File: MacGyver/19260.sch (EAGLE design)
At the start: 123 parts, among them J1 PST1,0/2-3,5, J10 RJ45J, J13 S04B, J2 PPPC101LFBN, J3 PPPC101LFBN, J4 PPPC101LFBN, J7 Pi Zero, J8 PST1,0/3-3,5, J9 RJ45J, Q1 IRFR5305, Q10 K38, Q11 K38, Q2 K1N, Q201 K1N, Q202 K1N, Q203 K1N, Q3 IRFR5305, Q4 P65, Q5 K3N, Q6 K1N, Q7 K3N, Q8 P65, Q9 K38, U1 1087, U10 Z4, U2 1087, U203 THVD1500, U204 THVD1500, U205 THVD1500, U3 I50115, U4 I50115, U5 AVR128DA28-I/SP, U6 AVR128DB32-I/PT, U7 Z4, U8 Z4, U9 Z4

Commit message: MacGyver: starting layout
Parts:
- removed C16, C17, C204, C205: .1uF, C-C:CC0603A
- removed J13: S04B, J-HDR2mm:B04B
- removed Q202: K1N, Q-NPN:NPNSOT23
- removed R202, R27, R28: 10k, R-C:R0805
- removed R203: 1.82k, R-C:R0805
- removed R221, R23, R24, R25, R26: 3.01k, R-C:R0805
- removed R224: 100k, R-C:R0805
- removed R227: 10K, R-C:R0805
- removed U10, U9: Z4, U-7400:2G07SOT26
- added C103, C104, C106, C107: .1uF, C-C:CC0603A
- added C108, C109: 27pF, C-C:CC0603A
- added J5: Pi Zero, U-Pi:RPI-ZERO90
- added Q102: K1N, Q-NPN:NPNSOT23
- added R101, R117, R118: 10k, R-C:R0805
- added R102, R105, R106, R107: 3.01k, R-C:R0805
- added R103: 1.82k, R-C:R0805
- added R112: 100k, R-C:R0805
- added U101: Z4, U-7400:2G07SOT26
- added U106: AVR128DB32-I/PT, U-AVR:AVR128DB32
- added Y1: 16MHz, Y-XTL:CSM-3X
- J7: value Pi Zero -> S04B; device U-Pi:RPI-ZERO90 -> J-HDR2mm:B04B
- Q2: value K1N -> IRFR5305; device Q-NPN:NPNSOT23 -> Q-PCH:N-CHDPAK
- Q3: value IRFR5305 -> P65; device Q-PCH:N-CHDPAK -> Q-PCH:N-CHSOT23
- Q4: value P65 -> K3N; device Q-PCH:N-CHSOT23 -> Q-PNP:PNPSOT23
- Q5: value K3N -> K1N; device Q-PNP:PNPSOT23 -> Q-NPN:NPNSOT23
- Q6: value K1N -> K3N; device Q-NPN:NPNSOT23 -> Q-PNP:PNPSOT23
- Q7: value K3N -> P65; device Q-PNP:PNPSOT23 -> Q-PCH:N-CHSOT23
- Q8: value P65 -> K38; device Q-PCH:N-CHSOT23 -> Q-NCH:N-CHSOT23
- Q9: value K38 -> K1N; device Q-NCH:N-CHSOT23 -> Q-NPN:NPNSOT23
- R10: value 10k -> 80.6k
- R11: value 100k -> 10k
- R12: value 80.6k -> 100k
- R14: value 10k -> 49.9k
- R15: value 49.9k -> 10k
- R18: value 1.82k -> 10k
- R2: value 100k -> 0.010; device R-C:R0805 -> R-C:R1210
- R21: value 10k -> 3.01k
- R3: value 0.010 -> 1K; device R-C:R1210 -> R-C:R0805
- R4, R9: value 10k -> 100k
- R5: value 1K -> 15.8k
- R6: value 100k -> 0.068; device R-C:R0805 -> R-C:R1210
- R7: value 15.8k -> 10k
- R8: value 0.068 -> 10k; device R-C:R1210 -> R-C:R0805
- U5: value AVR128DA28-I/SP -> Z4; device U-AVR:AVR128DA28-I/SP -> U-7400:2G07SOT26
- U6: value AVR128DB32-I/PT -> AVR128DA28-I/SP; device U-AVR:AVR128DB32 -> U-AVR:AVR128DA28-I/SP
- renumbered C201 to C101, C202 to C102, C203 to C105, C208 to C110, D2 to D1, D202 to D101, J8 to J6, Q201 to Q101, Q203 to Q103, R212 to R108, R213 to R110, R214 to R104, R215 to R114, R222 to R109, R223 to R120, R225 to R111, R226 to R113, R229 to R124, R230 to R125, R231 to R126, R232 to R127, R233 to R119, R234 to R121, R235 to R122, R236 to R123, R237 to R116, R238 to R115, R239 to R128, U203 to U102, U204 to U104, U205 to U105, U8 to U103
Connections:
- removed net PI_RX0: J7.RXD/BCM15, R18.2, R203.1, U103B.O, U6.(TX1)PC0, U7B.O
- removed net PI_TX0: J7.TXD/BCM14, R202.2, U103A.I, U6.(RX1)PC1, U7A.I
- removed net UPDI-APP: J4.8, R26.1, U10B.I, U5.UPDI
- new net APP_UPDI: J3.8, R21.1, U6.UPDI, U7B.I
- new net PI_RX: J5.RXD/BCM15, R103.2, U101B.O, U103B.O, U106.(TX1)PC0
- new net PI_TX: J5.TXD/BCM14, R101.2, U101A.I, U103A.I, U106.(RX1)PC1
- net !RESET: now also J3.5, U6.PF6(!RESET); no longer J4.5, U5.PF6(!RESET)
- net !SS: now also J2.8, U6.(!SS!)PA7; no longer J3.8, U5.(!SS!)PA7
- net +5V: now also C106.1, C107.1, C14.1, J7.3, R102.1, R105.1, R20.1, R8.2, U106.AVDD, U106.VDD, U6.AVCC, U6.VCC@0; no longer C12.1, C204.1, C205.1, J13.3, R10.2, R227.1, R23.1, R24.1, R25.1, U5.AVCC, U5.VCC@0, U6.AVDD, U6.VDD
- net +5V_2PI: now also J5.5V0@1, J5.5V0@2; no longer J7.5V0@1, J7.5V0@2
- net 0V: now also C103.2, C104.2, C106.2, C107.2, C108.1, C109.1, J5.GND@1, J5.GND@2, J5.GND@3, J5.GND@4, J5.GND@5, J5.GND@6, J5.GND@7, J5.GND@8, J7.4, Q102.E, Q8.S, R107.1, R11.1, R117.2, R118.2, R13.2, R18.2, R5.1, U101P.GND, U106.0V@0, U106.0V@1, U5P.GND; no longer C16.2, C17.2, C204.2, C205.2, J13.4, J7.GND@1, J7.GND@2, J7.GND@3, J7.GND@4, J7.GND@5, J7.GND@6, J7.GND@7, J7.GND@8, Q202.E, Q9.S, R13.1, R14.2, R21.2, R221.1, R27.2, R28.2, R7.1, U10P.GND, U5.0V@0, U5.0V@1, U9P.GND
- net AIN0: now also J4.3, U6.(AIN0)PD0; no longer J2.3, U5.(AIN0)PD0
- net AIN1: now also J4.4, U6.(AIN1)PD1; no longer J2.4, U5.(AIN1)PD1
- net AIN2: now also J4.5, U6.(AIN2)PD2; no longer J2.5, U5.(AIN2)PD2
- net AIN3: now also J4.6, U6.(AIN3)PD3; no longer J2.6, U5.(AIN3)PD3
- net AIN4: now also J4.7, U6.(AIN4)PD4; no longer J2.7, U5.(AIN4)PD4
- net AIN5: now also J4.8, U6.(AIN5)PD5; no longer J2.8, U5.(AIN5)PD5
- net AIN6: now also J4.9, U6.(AIN6)PD6; no longer J2.9, U5.(AIN6)PD6
- net AIN7: now also J4.10, U6.(AREF)PD7; no longer J2.10, U5.(AREF)PD7
- net ALT_EN: now also R13.1, U106.(AIN5)PD5; no longer R14.1, U6.(AIN5)PD5
- net ALT_I: now also R15.1, U106.(AIN1)PD1; no longer R4.1, U6.(AIN1)PD1
- net ALT_V: now also R11.2, U106.(AIN2)PD2; no longer R13.2, U6.(AIN2)PD2
- net APP_RX0: now also J3.7, R17.2, U5A.O, U6.(RX0)PA1; no longer J4.7, R23.2, U5.(RX0)PA1, U9A.O
- net APP_TX0: now also J3.6, U5B.I, U6.(EXTCLK/TX0)PA0; no longer J4.6, U5.(EXTCLK/TX0)PA0, U9B.I
- net APP_UART_: now also C12.1, R18.1, U106.(SDA0)PA2, U5P.VCC; no longer C16.1, R27.1, U6.(SDA0)PA2, U9P.VCC
- net APP_UPDI_: now also C15.1, R22.1, U106.(SCL0)PA3, U7P.VCC; no longer C17.1, R28.1, U10P.VCC, U6.(SCL0)PA3
- net FROM_RPU_OOB: now also U106.PF1(RX2); no longer U6.PF1(RX2)
- net FROM_RPU_RX: now also U5A.I, U7A.I; no longer U10A.I, U9A.I
- net FROM_RPU_TX: now also U101B.I; no longer U7B.I
- net I2C_SCL: now also J2.4, J7.1, U6.(SCL0)PA3; no longer J13.1, J3.4, U5.(SCL0)PA3
- net I2C_SCL_: now also U106.PF3(SCL1); no longer U6.PF3(SCL1)
- net I2C_SDA: now also J2.3, J7.2, U6.(SDA0)PA2; no longer J13.2, J3.3, U5.(SDA0)PA2
- net I2C_SDA_: now also U106.PF2(SDA1); no longer U6.PF2(SDA1)
- net MGR_LED: now also U106.(AREF)PD7; no longer U6.(AREF)PD7
- net MGR_UPDI: now also R106.1, U106.UPDI; no longer R20.1, U6.UPDI
- net MISO: now also J2.6, U6.(MISO)PA5; no longer J3.6, U5.(MISO)PA5
- net MOSI: now also J2.5, U6.(MOSI)PA4; no longer J3.5, U5.(MOSI)PA4
- net N$1: now also R105.2, R106.2; no longer R19.2, R20.2
- net N$10: now also Q4.E, Q6.B, R3.1; no longer Q5.E, Q7.B, R5.1
- net N$11: now also C109.2, U106.PA0(XTALHF1), Y1.2; no longer U6.PA0(XTALHF1)
- net N$2: now also Q7.G, R10.1, R9.2; no longer Q8.G, R11.2, R12.1
- net N$3: now also R20.2, R21.2, U7A.O; no longer R25.2, R26.2, U10A.O
- net N$32: now also Q2.S, Q9.E, R12.2, R2.1; no longer Q2.E, Q3.S, R2.2, R3.1
- net N$33: now also Q2.G, Q9.B, Q9.C, R12.1, R14.2; no longer Q2.B, Q2.C, Q3.G, R15.2, R2.1
- net N$34: now also R14.1; no longer R15.1
- net N$4: now also Q8.D, R10.2; no longer Q9.D, R12.2
- net N$5: now also Q4.B, Q6.C; no longer Q5.B, Q7.C
- net N$6: now also Q3.G, Q5.B, Q5.C, Q6.E, R3.2; no longer Q4.G, Q6.B, Q6.C, Q7.E, R5.2
- net N$65: now also R15.2; no longer R4.2
- net N$66: now also R2.2; no longer R3.2
- net N$7: now also Q4.C; no longer Q5.C
- net N$8: now also R7.2; no longer R9.2
- net N$83: now also Q102.C; no longer Q202.C
- net N$84: now also Q102.B, R112.1; no longer Q202.B, R224.1
- net N$9: now also C108.2, U106.PA1(XTALHF2), Y1.1; no longer U6.PA1(XTALHF2)
- net OOB_!RE: now also R107.2, U106.(SCK)PA6; no longer R221.2, U6.(SCK)PA6
- net OOB_DE: now also U106.(!SS!)PA7; no longer U6.(!SS!)PA7
- net PC2: now also J3.9, U6.PC2; no longer J4.9, U5.PC2
- net PC3: now also J3.10, U6.PC3; no longer J4.10, U5.PC3
- net PI3V3: now also J5.3V3@1, R101.1, R103.1, U106.VDDIO2; no longer J7.3V3@1, R18.1, R202.1, R203.2, U6.VDDIO2
- net PIPWR_EN: now also Q8.G, R8.1, U106.(AIN6)PD6; no longer Q9.G, R10.1, U6.(AIN6)PD6
- net PI_UART_TO_MGR_UPDI: now also C104.1, J5.SD_DAT0/BCM24, R118.1; no longer C15.1, J7.SD_DAT0/BCM24, R22.1
- net PI_UART_TO_RPU: now also C103.1, J5.SD_CMD/BCM23, R117.1, U101P.VCC; no longer C14.1, J7.SD_CMD/BCM23, R21.1, U7P.VCC
- net POWER: now also Q2.D; no longer Q4.D
- net PWR_I: now also R7.1, U106.(AIN3)PD3; no longer R9.1, U6.(AIN3)PD3
- net PWR_V: now also R4.1, R5.2, U106.(AIN4)PD4; no longer R6.1, R7.2, U6.(AIN4)PD4
- net RX1: now also J2.10, U6.(RX1)PC1; no longer J3.10, U5.(RX1)PC1
- net RX2: now also J3.4, U6.PF1(RX2); no longer J4.4, U5.PF1(RX2)
- net RX_!RE: now also U106.(MOSI)PA4; no longer U6.(MOSI)PA4
- net RX_DE: now also U106.PF4(AIN20); no longer U6.PF4(AIN20)
- net RX_RPU: no longer R227.2
- net SCK: now also J2.7, U6.(SCK)PA6; no longer J3.7, U5.(SCK)PA6
- net SHLD_VIN: now also Q7.D; no longer Q8.D
- net SHUTDWN: now also U106.PF6(!RESET); no longer U6.PF6(!RESET)
- net SHUTDWN_TO_BCM6: now also J5.BCM6; no longer J7.BCM6
- net SMBUS_SCL: now also J5.BCM3/SCL, U106.(*SCL0)PC3; no longer J7.BCM3/SCL, U6.(*SCL0)PC3
- net SMBUS_SDA: now also J5.BCM2/SDA, U106.(*SDA0)PC2; no longer J7.BCM2/SDA, U6.(*SDA0)PC2
- net TO_RPU_OOB: now also R112.2, U106.PF0(TX2); no longer R224.2, U6.PF0(TX2)
- net TO_RPU_RX: now also R102.2, U101A.O; no longer R17.2, U7A.O
- net TO_RPU_TX: now also R19.2, U5B.O, U7B.O; no longer R24.2, U10B.O, U9B.O
- net TX1: now also J2.9, U6.(TX1)PC0; no longer J3.9, U5.(TX1)PC0
- net TX2: now also J3.3, U6.PF0(TX2); no longer J4.3, U5.PF0(TX2)
- net TX_!RE: now also U106.PF5(AIN21); no longer U6.PF5(AIN21)
- net TX_DE: now also U106.(MISO)PA5; no longer U6.(MISO)PA5
- net VIN: now also Q7.S, R6.1, R9.1; no longer Q8.S, R11.1, R8.1
- net VIN_S: now also Q3.S, Q5.E, R4.2; no longer Q4.S, Q6.E, R8.2
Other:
- note added: "R-PI TO MGR_UPDI"
- note added: "R-PI TO RPU"
- note added: "RPU TO APPLICATION"
- note added: "RPU TO APP_UPDI"
- note removed: "MGR UPDI TO R-PI"
- note removed: "RPU TX/RX TO R-PI"
- note removed: "UART_0 TO APPLICATION"

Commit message: MacGyver: layout wip
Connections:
- net ALT_EN: now also U106.(SCL0)PA3; no longer U106.(AIN5)PD5
- net APP_UART_: now also U106.PF4(AIN20); no longer U106.(SDA0)PA2
- net APP_UPDI_: now also U106.PF5(AIN21); no longer U106.(SCL0)PA3
- net PIPWR_EN: now also U106.(SDA0)PA2; no longer U106.(AIN6)PD6
- net RX_!RE: now also U106.(AIN5)PD5; no longer U106.(MOSI)PA4
- net RX_DE: now also U106.(AIN6)PD6; no longer U106.PF4(AIN20)
- net TX_!RE: now also U106.(MOSI)PA4; no longer U106.PF5(AIN21)
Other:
- note removed: "15"
- note removed: "2"
- note removed: "25"
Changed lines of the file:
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@@
 <text x="335.788" y="44.196" size="2.1844" layer="98">11/12/20</text>
 <text x="356.616" y="19.558" size="2.54" layer="98">MACGYVER</text>
-<text x="106.934" y="94.488" size="1.27" layer="98">2</text>
-<text x="106.934" y="51.308" size="1.27" layer="98">15</text>
 <text x="109.474" y="43.688" size="1.27" layer="98">17</text>
-<text x="51.054" y="58.928" size="1.27" layer="98">25</text>
 <text x="119.634" y="76.454" size="2.54" layer="98">debug</text>
 <text x="372.364" y="190.754" size="2.54" layer="98">OUT OF BAND</text>
@@
 <segment>
 <pinref part="C109" gate="G$1" pin="1"/>
-<wire x1="43.18" y1="76.2" x2="40.64" y2="76.2" width="0.1524" layer="91"/>
-<wire x1="40.64" y1="76.2" x2="40.64" y2="83.82" width="0.1524" layer="91"/>
+<wire x1="43.18" y1="76.2" x2="38.1" y2="76.2" width="0.1524" layer="91"/>
+<wire x1="38.1" y1="76.2" x2="38.1" y2="83.82" width="0.1524" layer="91"/>
 <pinref part="GND14" gate="1" pin="0V"/>
-<wire x1="40.64" y1="83.82" x2="43.18" y2="83.82" width="0.1524" layer="91"/>
+<wire x1="38.1" y1="83.82" x2="43.18" y2="83.82" width="0.1524" layer="91"/>
 <pinref part="C108" gate="G$1" pin="1"/>
-<wire x1="43.18" y1="86.36" x2="40.64" y2="86.36" width="0.1524" layer="91"/>
-<wire x1="40.64" y1="86.36" x2="40.64" y2="83.82" width="0.1524" layer="91"/>
-<junction x="40.64" y="83.82"/>
+<wire x1="43.18" y1="86.36" x2="38.1" y2="86.36" width="0.1524" layer="91"/>
+<wire x1="38.1" y1="86.36" x2="38.1" y2="83.82" width="0.1524" layer="91"/>
+<junction x="38.1" y="83.82"/>
 </segment>
 </net>
@@
 </segment>
 <segment>
-<label x="109.22" y="93.98" size="1.27" layer="91" xref="yes"/>
-<wire x1="99.06" y1="93.98" x2="109.22" y2="93.98" width="0.1524" layer="91"/>
-<pinref part="U106" gate="G$1" pin="(MOSI)PA4"/>
+<label x="109.22" y="50.8" size="1.27" layer="91" xref="yes"/>
+<wire x1="99.06" y1="50.8" x2="109.22" y2="50.8" width="0.1524" layer="91"/>
+<pinref part="U106" gate="G$1" pin="(AIN5)PD5"/>
 </segment>
 </net>
@@
 </segment>
 <segment>
-<label x="50.8" y="58.42" size="1.27" layer="91" rot="MR0" xref="yes"/>
-<wire x1="60.96" y1="58.42" x2="50.8" y2="58.42" width="0.1524" layer="91"/>
-<pinref part="U106" gate="G$1" pin="PF5(AIN21)"/>
+<label x="109.22" y="93.98" size="1.27" layer="91" rot="MR180" xref="yes"/>
+<wire x1="109.22" y1="93.98" x2="99.06" y2="93.98" width="0.1524" layer="91"/>
+<pinref part="U106" gate="G$1" pin="(MOSI)PA4"/>
 </segment>
 </net>
@@
 </segment>
 <segment>
-<label x="50.8" y="60.96" size="1.27" layer="91" rot="MR0" xref="yes"/>
-<wire x1="60.96" y1="60.96" x2="50.8" y2="60.96" width="0.1524" layer="91"/>
-<pinref part="U106" gate="G$1" pin="PF4(AIN20)"/>
+<label x="109.22" y="48.26" size="1.27" layer="91" rot="MR180" xref="yes"/>
+<wire x1="99.06" y1="48.26" x2="109.22" y2="48.26" width="0.1524" layer="91"/>
+<pinref part="U106" gate="G$1" pin="(AIN6)PD6"/>
 </segment>
 </net>
@@
 <net name="ALT_EN" class="0">
 <segment>
-<label x="109.22" y="50.8" size="1.27" layer="91" xref="yes"/>
-<wire x1="99.06" y1="50.8" x2="109.22" y2="50.8" width="0.1524" layer="91"/>
-<pinref part="U106" gate="G$1" pin="(AIN5)PD5"/>
+<label x="109.22" y="96.52" size="1.27" layer="91" xref="yes"/>
+<wire x1="99.06" y1="96.52" x2="109.22" y2="96.52" width="0.1524" layer="91"/>
+<pinref part="U106" gate="G$1" pin="(SCL0)PA3"/>
 </segment>
 </net>
@@
 <net name="PIPWR_EN" class="0">
 <segment>
-<label x="109.22" y="48.26" size="1.27" layer="91" xref="yes"/>
-<wire x1="99.06" y1="48.26" x2="109.22" y2="48.26" width="0.1524" layer="91"/>
-<pinref part="U106" gate="G$1" pin="(AIN6)PD6"/>
+<label x="109.22" y="99.06" size="1.27" layer="91" xref="yes"/>
+<wire x1="99.06" y1="99.06" x2="109.22" y2="99.06" width="0.1524" layer="91"/>
+<pinref part="U106" gate="G$1" pin="(SDA0)PA2"/>
 </segment>
 </net>
@@
 <segment>
 <label x="109.22" y="53.34" size="1.27" layer="91" xref="yes"/>
+<pinref part="U106" gate="G$1" pin="(AIN4)PD4"/>
 <wire x1="99.06" y1="53.34" x2="109.22" y2="53.34" width="0.1524" layer="91"/>
-<pinref part="U106" gate="G$1" pin="(AIN4)PD4"/>
 </segment>
 </net>
@@
 <net name="APP_UART_" class="0">
 <segment>
-<pinref part="U106" gate="G$1" pin="(SDA0)PA2"/>
-<wire x1="99.06" y1="99.06" x2="109.22" y2="99.06" width="0.1524" layer="91"/>
-<label x="109.22" y="99.06" size="1.27" layer="91" xref="yes"/>
+<label x="50.8" y="60.96" size="1.27" layer="91" rot="R180" xref="yes"/>
+<wire x1="60.96" y1="60.96" x2="50.8" y2="60.96" width="0.1524" layer="91"/>
+<pinref part="U106" gate="G$1" pin="PF4(AIN20)"/>
 </segment>
 </net>
 <net name="APP_UPDI_" class="0">
 <segment>
-<pinref part="U106" gate="G$1" pin="(SCL0)PA3"/>
-<wire x1="99.06" y1="96.52" x2="109.22" y2="96.52" width="0.1524" layer="91"/>
-<label x="109.22" y="96.52" size="1.27" layer="91" xref="yes"/>
-</segment>
-</net>
+<label x="50.8" y="58.42" size="1.27" layer="91" rot="R180" xref="yes"/>
+<wire x1="50.8" y1="58.42" x2="60.96" y2="58.42" width="0.1524" layer="91"/>
+<pinref part="U106" gate="G$1" pin="PF5(AIN21)"/>
+</segment>
+</net>

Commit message: MacGyver: layout wip++
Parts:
- removed TP2, TP3: TPPAD1-08, J-TP:TPPAD1-08
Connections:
- net N$1 renamed MGR_UPDI_PULLUP
- net N$3 renamed APP_UPDI_PULLUP
- net I2C_SCL: no longer TP2.TP
- net I2C_SDA: no longer TP1.TP
- net MGR_UPDI: now also TP1.TP; no longer TP3.TP
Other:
- moved on the sheet: TP1
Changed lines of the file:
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@@
 <part name="Q1" library="Q-PCH" deviceset="N-CH?*" device="DPAK" value="IRFR5305"/>
 <part name="Q11" library="Q-NCH" deviceset="N-CH?*" device="SOT23" value="K38"/>
-<part name="TP1" library="J-TP" deviceset="TP" device="PAD1-08"/>
-<part name="TP2" library="J-TP" deviceset="TP" device="PAD1-08"/>
 <part name="J4" library="J-HDR2.54mm" deviceset="F1X10" device="" value="PPPC101LFBN"/>
 <part name="J2" library="J-HDR2.54mm" deviceset="F1X10" device="" value="PPPC101LFBN"/>
@@
 <part name="R18" library="R-C" deviceset="R" device="0805" value="10k"/>
 <part name="R22" library="R-C" deviceset="R" device="0805" value="10k"/>
-<part name="TP3" library="J-TP" deviceset="TP" device="PAD1-08"/>
+<part name="TP1" library="J-TP" deviceset="TP" device="PAD1-08"/>
 <part name="R19" library="R-C" deviceset="R" device="0805" value="3.01k"/>
 <part name="P+10" library="Plane" deviceset="+5V" device=""/>
@@
 </segment>
 </net>
-<net name="N$3" class="0">
+<net name="APP_UPDI_PULLUP" class="0">
 <segment>
 <pinref part="U7" gate="A" pin="O"/>
@@
 <instance part="P+29" gate="1" x="121.92" y="27.94"/>
 <instance part="P+31" gate="1" x="210.82" y="86.36"/>
-<instance part="TP1" gate="G$1" x="215.9" y="78.74"/>
-<instance part="TP2" gate="G$1" x="215.9" y="68.58"/>
 <instance part="GND1" gate="1" x="22.86" y="83.82"/>
 <instance part="GND4" gate="1" x="30.48" y="81.28"/>
@@
 <instance part="R117" gate="G$1" x="86.36" y="137.16" rot="R270"/>
 <instance part="R118" gate="G$1" x="124.46" y="137.16" rot="R270"/>
-<instance part="TP3" gate="G$1" x="58.42" y="93.98"/>
+<instance part="TP1" gate="G$1" x="58.42" y="93.98"/>
 <instance part="C108" gate="G$1" x="45.72" y="86.36" smashed="yes" rot="R90">
 <attribute name="NAME" x="48.006" y="86.995" size="1.778" layer="95"/>
@@
 <segment>
 <label x="220.98" y="73.66" size="1.27" layer="91" xref="yes"/>
-<wire x1="220.98" y1="73.66" x2="215.9" y2="73.66" width="0.1524" layer="91"/>
 <pinref part="R126" gate="G$1" pin="1"/>
-<wire x1="215.9" y1="73.66" x2="198.12" y2="73.66" width="0.1524" layer="91"/>
+<wire x1="220.98" y1="73.66" x2="198.12" y2="73.66" width="0.1524" layer="91"/>
 <wire x1="198.12" y1="73.66" x2="195.58" y2="73.66" width="0.1524" layer="91"/>
 <wire x1="198.12" y1="78.74" x2="198.12" y2="73.66" width="0.1524" layer="91"/>
 <junction x="198.12" y="73.66"/>
 <pinref part="R124" gate="G$1" pin="1"/>
-<pinref part="TP1" gate="G$1" pin="TP"/>
-<wire x1="215.9" y1="76.2" x2="215.9" y2="73.66" width="0.1524" layer="91"/>
-<junction x="215.9" y="73.66"/>
 </segment>
 </net>
@@
 <segment>
 <label x="220.98" y="63.5" size="1.27" layer="91" xref="yes"/>
-<wire x1="220.98" y1="63.5" x2="215.9" y2="63.5" width="0.1524" layer="91"/>
-<wire x1="215.9" y1="63.5" x2="198.12" y2="63.5" width="0.1524" layer="91"/>
+<wire x1="220.98" y1="63.5" x2="198.12" y2="63.5" width="0.1524" layer="91"/>
 <wire x1="198.12" y1="63.5" x2="195.58" y2="63.5" width="0.1524" layer="91"/>
 <pinref part="R127" gate="G$1" pin="1"/>
@@
 <junction x="198.12" y="63.5"/>
 <pinref part="R125" gate="G$1" pin="1"/>
-<pinref part="TP2" gate="G$1" pin="TP"/>
-<wire x1="215.9" y1="66.04" x2="215.9" y2="63.5" width="0.1524" layer="91"/>
-<junction x="215.9" y="63.5"/>
 </segment>
 </net>
@@
 <label x="55.88" y="91.44" size="1.27" layer="91" rot="R180" xref="yes"/>
 <wire x1="60.96" y1="91.44" x2="58.42" y2="91.44" width="0.1524" layer="91"/>
-<pinref part="TP3" gate="G$1" pin="TP"/>
+<pinref part="TP1" gate="G$1" pin="TP"/>
 <wire x1="58.42" y1="91.44" x2="55.88" y2="91.44" width="0.1524" layer="91"/>
 <junction x="58.42" y="91.44"/>
@@
 </segment>
 </net>
-<net name="N$1" class="0">
+<net name="MGR_UPDI_PULLUP" class="0">
 <segment>
 <pinref part="U103" gate="A" pin="O"/>

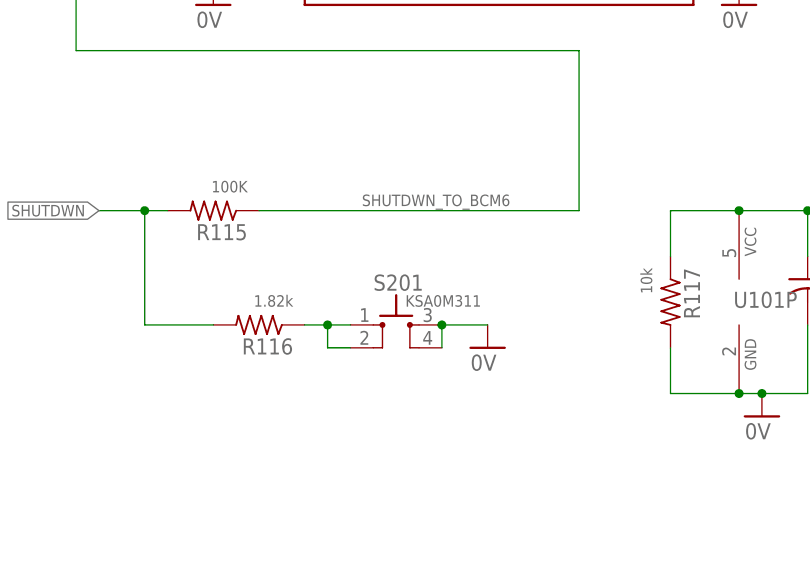
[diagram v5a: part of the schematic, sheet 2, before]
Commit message: macgyver: layout done, needs reviewing
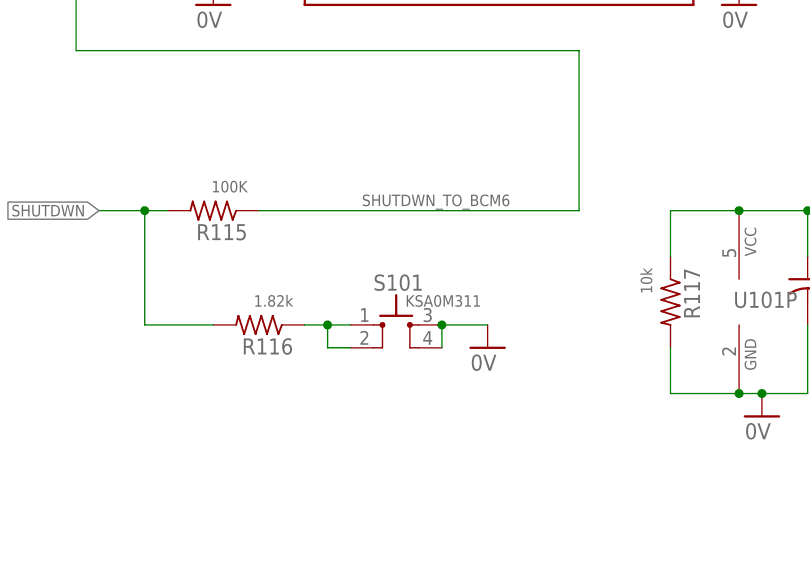
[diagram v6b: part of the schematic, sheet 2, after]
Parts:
- renumbered S201 to S101
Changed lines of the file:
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@@
 <part name="GND59" library="Plane" deviceset="0V" device=""/>
 <part name="GND60" library="Plane" deviceset="0V" device=""/>
-<part name="S201" library="S-Tactile" deviceset="KSA" device="0M311" value="KSA0M311"/>
+<part name="S101" library="S-Tactile" deviceset="KSA" device="0M311" value="KSA0M311"/>
 <part name="R116" library="R-C" deviceset="R" device="0805" value="1.82k"/>
 <part name="GND61" library="Plane" deviceset="0V" device=""/>
@@
 <instance part="C107" gate="G$1" x="30.48" y="91.44"/>
 <instance part="GND57" gate="1" x="40.64" y="45.72"/>
-<instance part="S201" gate="S" x="55.88" y="134.62"/>
+<instance part="S101" gate="S" x="55.88" y="134.62"/>
 <instance part="R116" gate="G$1" x="40.64" y="134.62" rot="R180"/>
 <instance part="GND61" gate="1" x="66.04" y="132.08"/>
@@
 </segment>
 <segment>
-<pinref part="S201" gate="S" pin="3"/>
+<pinref part="S101" gate="S" pin="3"/>
 <wire x1="60.96" y1="134.62" x2="66.04" y2="134.62" width="0.1524" layer="91"/>
 <pinref part="GND61" gate="1" pin="0V"/>
-<pinref part="S201" gate="S" pin="4"/>
+<pinref part="S101" gate="S" pin="4"/>
 <wire x1="60.96" y1="132.08" x2="60.96" y2="134.62" width="0.1524" layer="91"/>
 <junction x="60.96" y="134.62"/>
@@
 <net name="N$93" class="0">
 <segment>
-<pinref part="S201" gate="S" pin="2"/>
+<pinref part="S101" gate="S" pin="2"/>
 <wire x1="45.72" y1="134.62" x2="48.26" y2="134.62" width="0.1524" layer="91"/>
 <wire x1="48.26" y1="134.62" x2="48.26" y2="132.08" width="0.1524" layer="91"/>
 <wire x1="48.26" y1="132.08" x2="50.8" y2="132.08" width="0.1524" layer="91"/>
-<pinref part="S201" gate="S" pin="1"/>
+<pinref part="S101" gate="S" pin="1"/>
 <wire x1="50.8" y1="134.62" x2="48.26" y2="134.62" width="0.1524" layer="91"/>
 <junction x="48.26" y="134.62"/>

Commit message: notes
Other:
- note added: "ALT (CHARGING) POWER"
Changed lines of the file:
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@@
 <text x="182.372" y="230.886" size="1.778" layer="98">PWR_V</text>
 <text x="221.488" y="233.426" size="1.778" layer="98">PWR_I</text>
-<text x="10.922" y="212.852" size="1.778" layer="98">ALTERNATE POWER</text>
+<text x="8.382" y="212.852" size="1.778" layer="98">ALT (CHARGING) POWER</text>
 <text x="58.166" y="187.706" size="1.778" layer="98">ALTERNATE
 POWER</text>
